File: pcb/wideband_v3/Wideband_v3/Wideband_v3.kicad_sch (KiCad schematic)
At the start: 19 parts, among them J4 FT_CAN, J5 Conn_01x12, U10 LMV358, U4 TJA1051T-3, U7 MCP42010, U9 LMV358

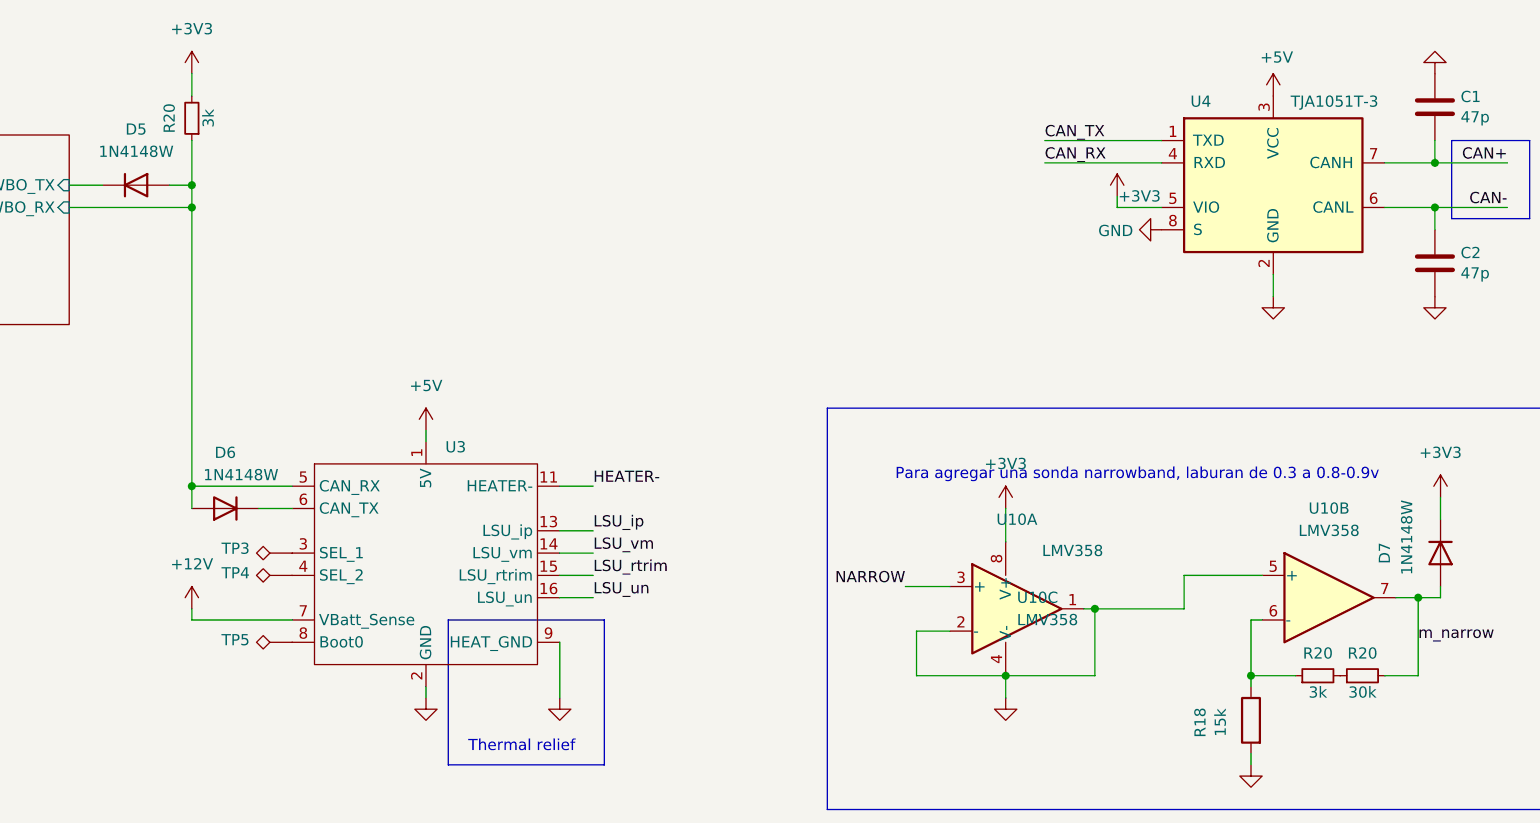
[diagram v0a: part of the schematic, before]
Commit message: Optimize SKUs
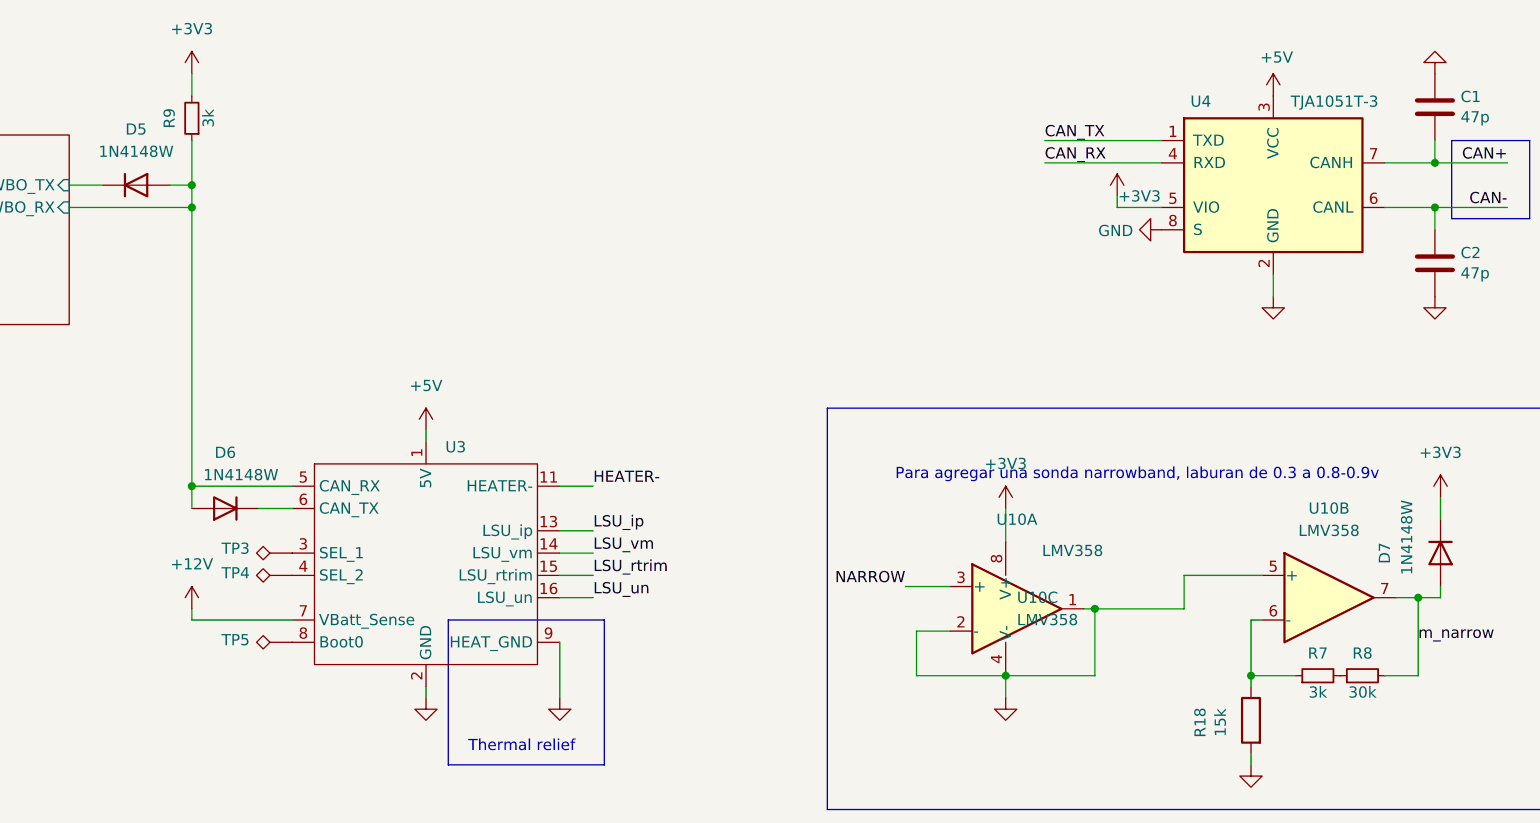
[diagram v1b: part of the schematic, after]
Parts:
- renumbered R20 to R7, R20 to R8, R20 to R9
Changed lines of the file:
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@@
 		(on_board yes)
 		(dnp no)
-		(property "Reference" "R20"
+		(property "Reference" "R7"
 			(at 233.68 92.71 90)
 			(effects
@@
 		(instances
 			(project "Wideband_v3"
-				(path "/08893845-3ad0-4661-81a4-b965d2c3e6dc/8f3b37b5-db17-4488-aba9-8d1ed80a11d5"
-					(reference "R20")
-					(unit 1)
-				)
 				(path "/08893845-3ad0-4661-81a4-b965d2c3e6dc"
 					(reference "R7")
@@
 		(on_board yes)
 		(dnp no)
-		(property "Reference" "R20"
+		(property "Reference" "R9"
 			(at 102.87 31.75 90)
 			(effects
@@
 		(instances
 			(project "Wideband_v3"
-				(path "/08893845-3ad0-4661-81a4-b965d2c3e6dc/8f3b37b5-db17-4488-aba9-8d1ed80a11d5"
-					(reference "R20")
-					(unit 1)
-				)
 				(path "/08893845-3ad0-4661-81a4-b965d2c3e6dc"
 					(reference "R9")
@@
 		(on_board yes)
 		(dnp no)
-		(property "Reference" "R20"
+		(property "Reference" "R8"
 			(at 238.76 92.71 90)
 			(effects
@@
 		(instances
 			(project "Wideband_v3"
-				(path "/08893845-3ad0-4661-81a4-b965d2c3e6dc/8f3b37b5-db17-4488-aba9-8d1ed80a11d5"
-					(reference "R20")
-					(unit 1)
-				)
 				(path "/08893845-3ad0-4661-81a4-b965d2c3e6dc"
 					(reference "R8")

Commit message: update DAC for v3
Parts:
- removed U7: MCP42010, Package_SO:SOIC-14_3.9x8.7mm_P1.27mm, symbol Potentiometer_Digital:MCP42010
- added U5, U6: TPL0401A-10-Q1, Package_TO_SOT_SMD:Texas_R-PDSO-G6, symbol Potentiometer_Digital:TPL0401A-10-Q1
- J4, J5, TP3, TP4, TP5: now left out of the parts list
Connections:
- net +5V: now also U5.1 (VDD), U5.6 (H), U6.1 (VDD), U6.6 (H)
- net GND: now also U5.2 (GND), U6.2 (GND)
- net m_LAMBDA_OUT: now also U6.5 (W)
- net m_TEMP_OUT: now also U5.5 (W)
- new net DAC_CLK_1: U5.3 (SCL)
- new net DAC_CLK_2: U6.3 (SCL)
- new net DAC_SDA_1: U5.4 (SDA)
- new net DAC_SDA_2: U6.4 (SDA)
- no-connect marks 2 -> 0
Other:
- sheet MCU ports: added DACK_SDA_2, DAC_CLK_1, DAC_CLK_2, DAC_SDA_1; removed DACK_SI, DAC_CS, DAC_SCK, DAC_SO

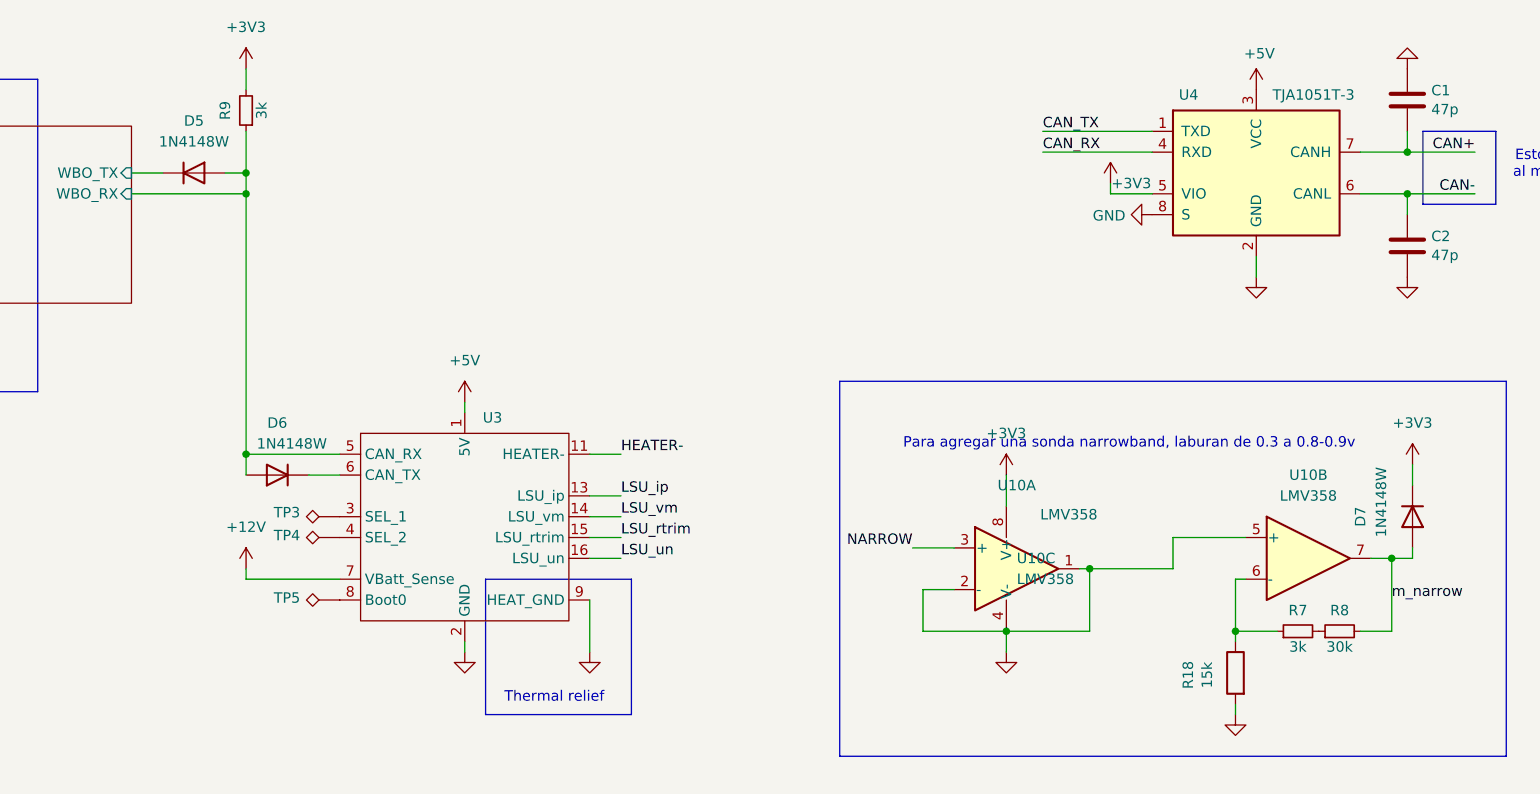
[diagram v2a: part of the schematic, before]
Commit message: update LCSC/Stock codes, update pcb to new footprints
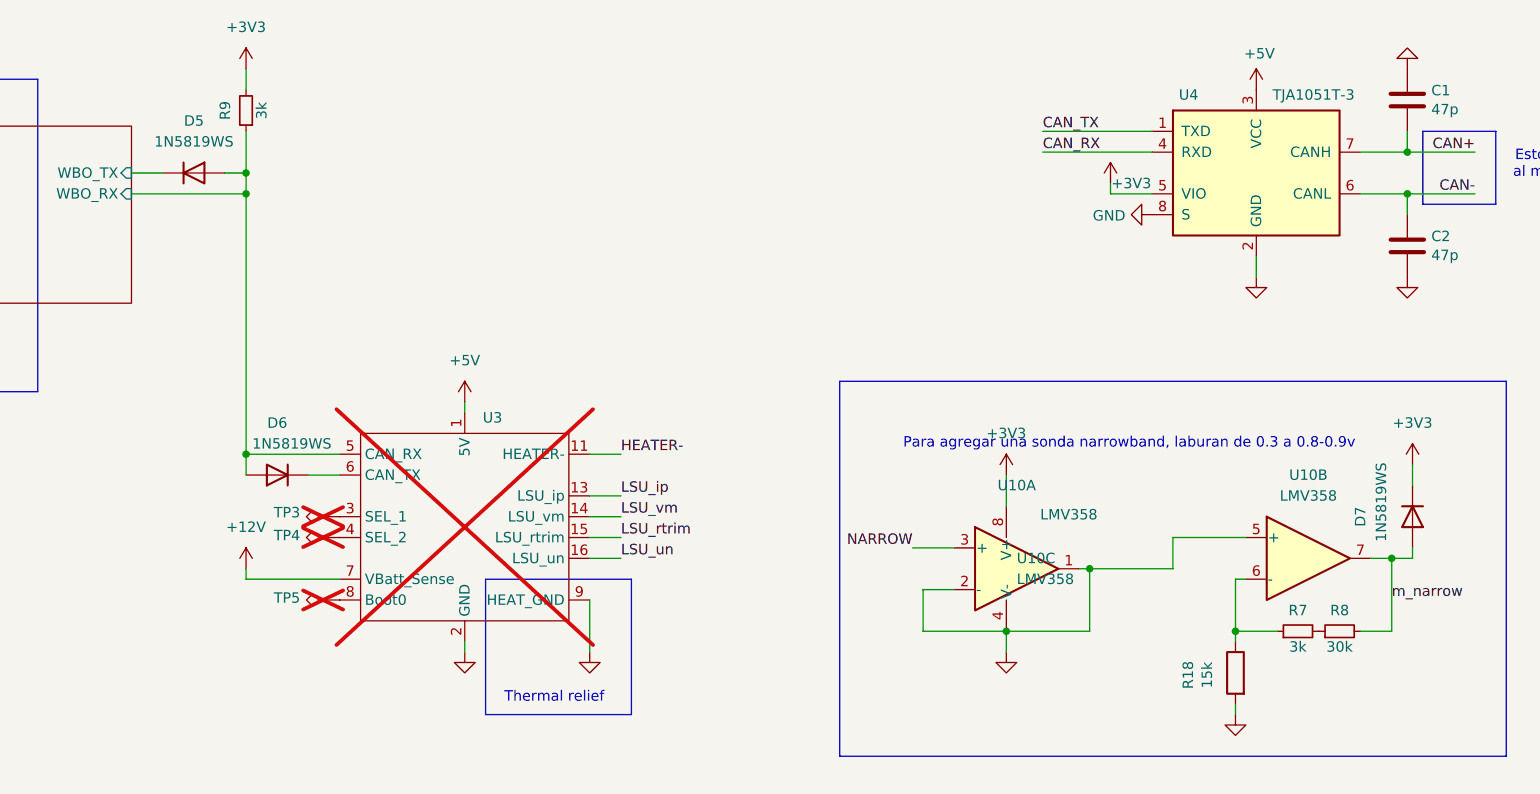
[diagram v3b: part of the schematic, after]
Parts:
- C1, C2: footprint Capacitor_SMD:C_0402_1005Metric -> Capacitor_SMD:C_0603_1608Metric; LCSC C1567 -> C105622; STOCK (none) -> CAP-000395-00
- D5, D6, D7: value 1N4148W -> 1N5819WS; LCSC (none) -> C191023; STOCK (none) -> DIO-000272-00
- J4: STOCK (none) -> CON-000413-00
- J5: LCSC (none) -> -; STOCK (none) -> CON-000412-00
- R18: LCSC (none) -> C100780; STOCK (none) -> RES-000224-00
- R7, R9: STOCK (none) -> RES-000402-00
- R8: STOCK (none) -> RES-000403-00
- TP3, TP4, TP5: LCSC (none) -> -; STOCK (none) -> -; now not fitted
- U10, U9: STOCK (none) -> ICS-000406-00
- U3: now not fitted
- U4: STOCK (none) -> ICS-000359-00
- U5, U6: STOCK (none) -> RES-000405-00
